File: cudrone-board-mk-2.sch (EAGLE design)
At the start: 44 parts, among them Q1 BSS138, U1 EDISON_CONNECTOR_FULLMOUNTING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, U2 FTS31XS-U, U4 TPS62065, U5 USD-SOCKETNEW, U6 TXB0108

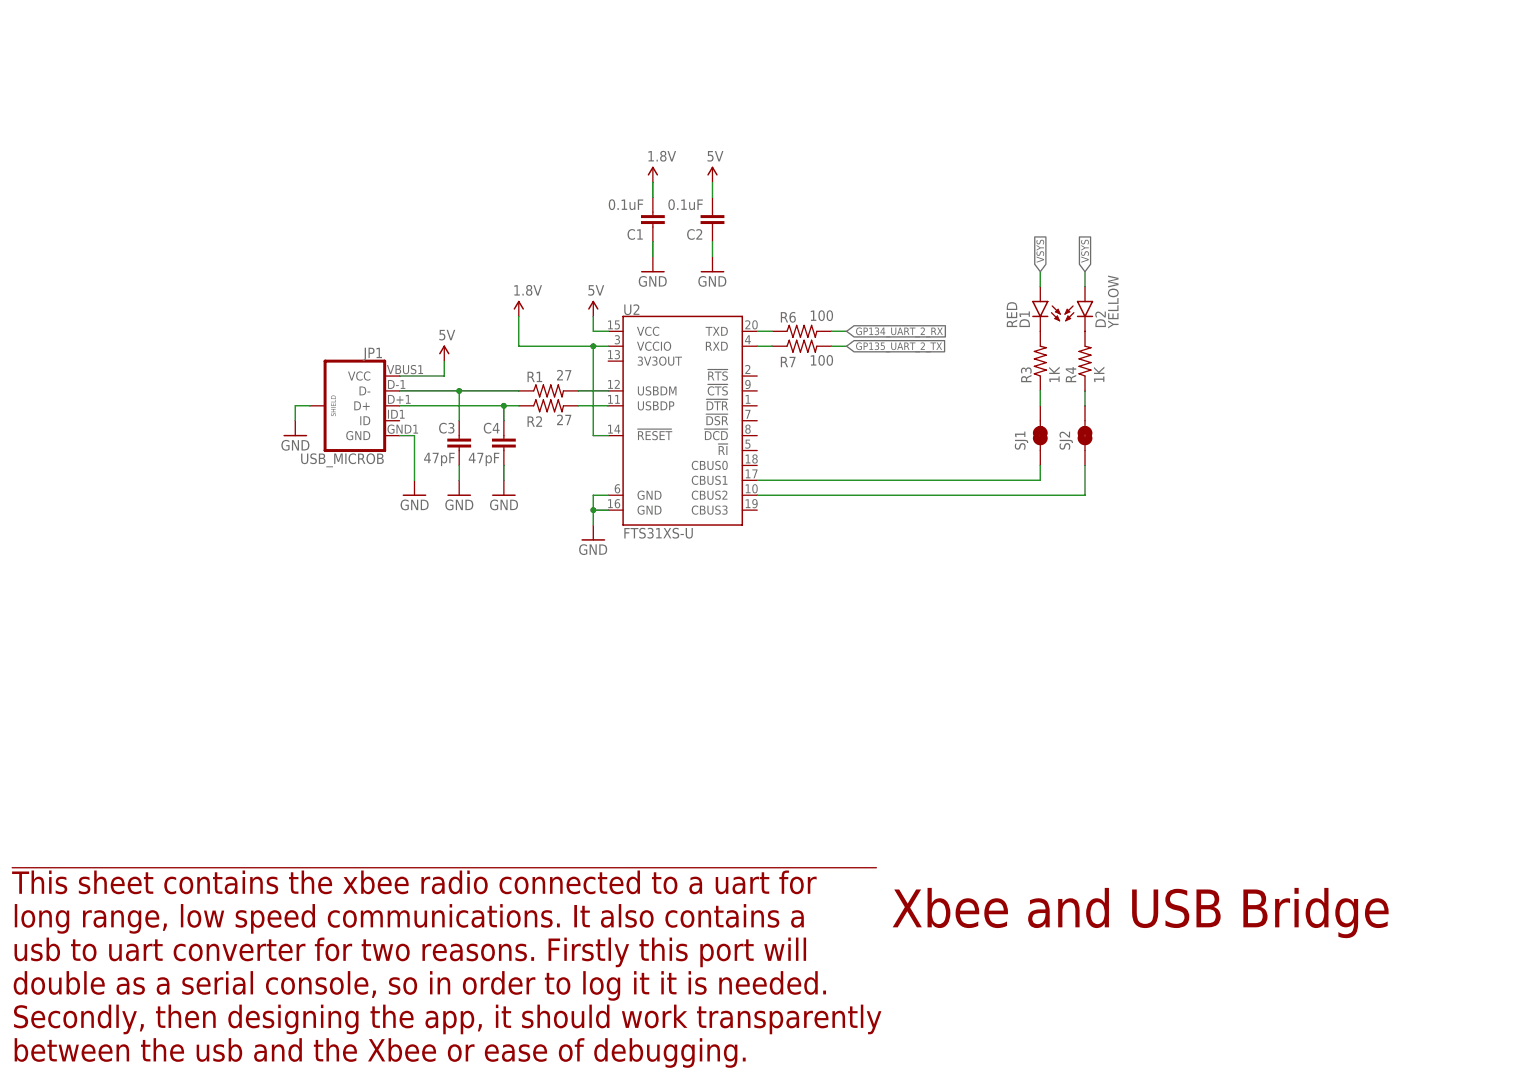
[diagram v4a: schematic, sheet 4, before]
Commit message: Added the rest of the sparkfun stuff
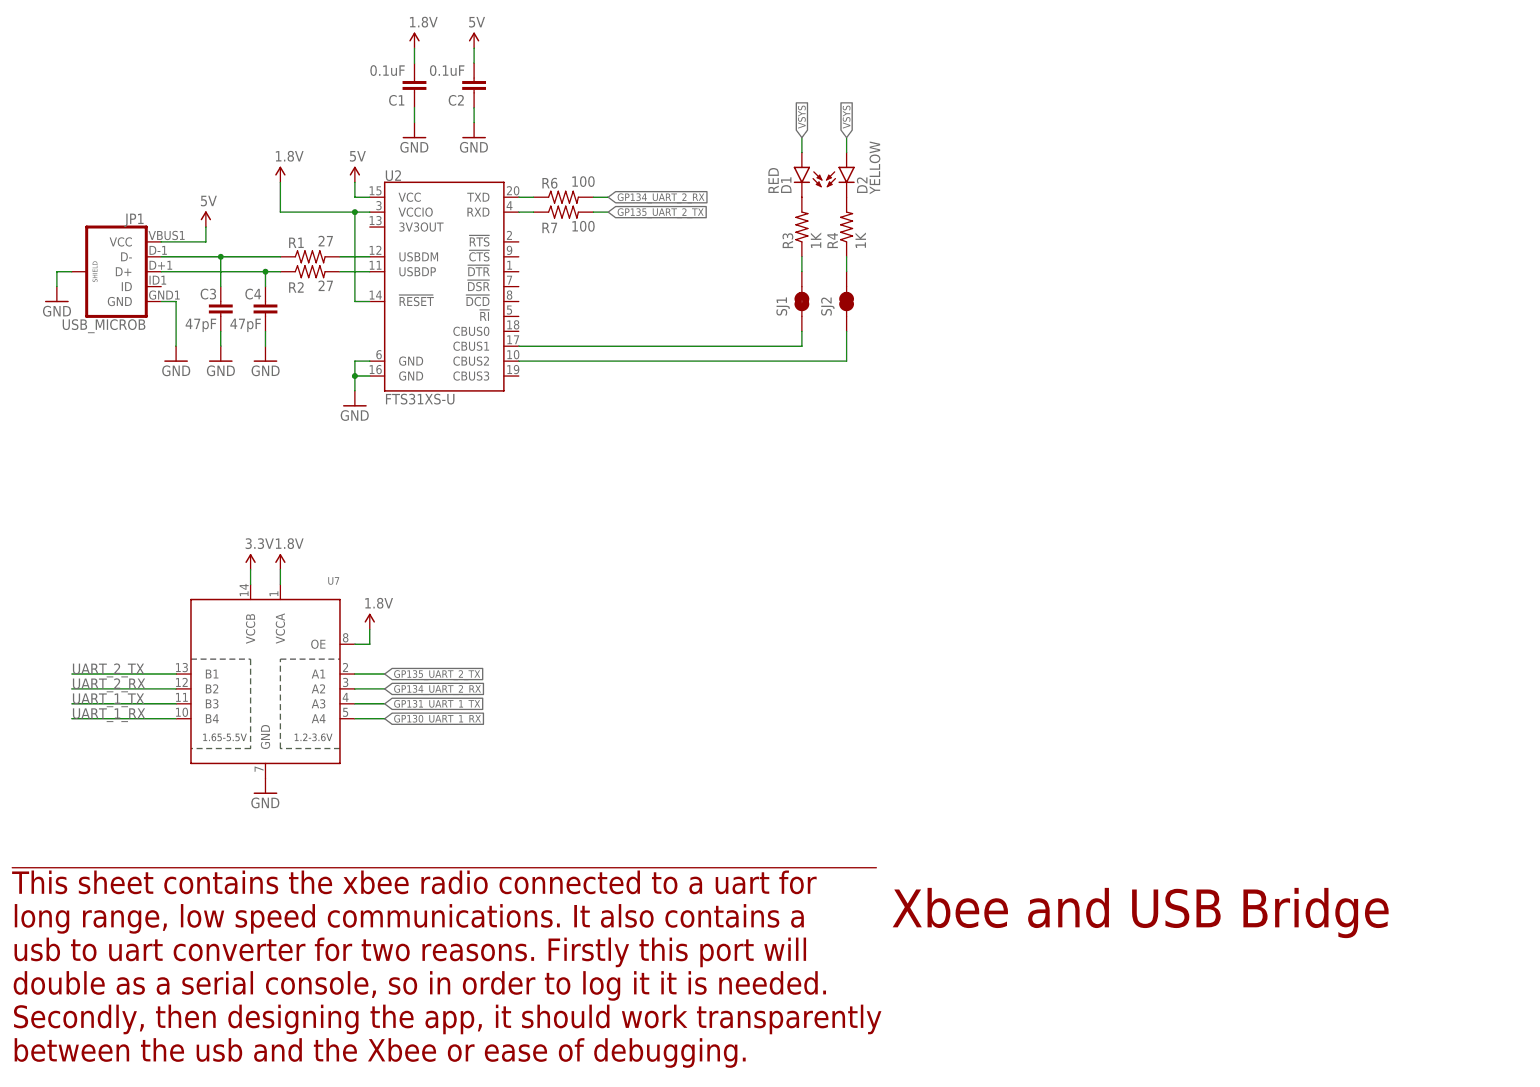
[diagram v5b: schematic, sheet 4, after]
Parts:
- added C11, C12: 0.1uF, SparkFun-Capacitors:0.1UF-25V(+80/-20%)(0603)
- added C13, C14: 10uF, SparkFun-Capacitors:10UF-6.3V-20%(1206)
- added JP2: (no value), SparkFun-Connectors:M04SMD_RA_FEMALE
- added R16, R17: 10K, SparkFun-Resistors:10KOHM1/10W1%(0603)0603
- added R18: 200k, SparkFun-Resistors:200KOHM1/10W1%(0603)200K
- added R19, R20: DNP, SparkFun-Resistors:2.2KOHM1/10W1%(0603)
- added SJ4: Power Select, SparkFun-Passives:JUMPER-PAD-3-2OF3_NC_BY_TRACE
- added U7: (no value), SparkFun-DigitalIC:TXB0104PWRSOIC14
- added U8: PCA9306, SparkFun-DigitalIC:PCA9306PCA9306DC-1:1
- added U9: MIC5205, SparkFun-PowerIC:MIC52053.3V
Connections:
- new net 3.3V-REGULATED: C14.1, SJ4.3, U9.OUT
- new net HV_SCL: JP2.1, R17.1, U8.SCL2
- new net HV_SDA: JP2.2, R16.1, U8.SDA2
- new net N$25: R18.1, U8.EN, U8.VREF2
- new net UART_1_RX: U7.B4
- new net UART_1_TX: U7.B3
- new net UART_2_RX: U7.B2
- new net UART_2_TX: U7.B1
- new net VOUT: C12.1, JP2.3, R16.2, R17.2, R18.2, SJ4.2
- net 1.8V: now also C11.1, R19.2, R20.2, U7.OE, U7.VCCA, U8.VREF1
- net 3.3V: now also U7.VCCB
- net GND: now also C11.2, C12.2, C13.2, C14.2, JP2.4, U7.GND, U8.GND, U9.GND
- net GP130_UART_1_RX: now also U7.A4
- net GP131_UART_1_TX: now also U7.A3
- net GP134_UART_2_RX: now also U7.A2
- net GP135_UART_2_TX: now also U7.A1
- net GP19_I2C_1_SCL: now also R19.1, U8.SCL1
- net GP20_I2C_1_SDA: now also R20.1, U8.SDA1
- net VSYS: now also C13.1, SJ4.1, U9.EN, U9.IN
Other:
- note added: "Note: Default VOUT is 3.3v regulated."
- moved on the sheet: C1, C2, C3, C4, D1, D2, JP1, R1, R2, R3, R4, R6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
